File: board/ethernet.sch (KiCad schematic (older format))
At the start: 61 parts, among them IC5 KSZ8081RNx, IC6 MAX5969x, IC7 MAX17503, J1 RJHSE-538B, T1 749010012A, Y2 25MHz

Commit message: Made capacitors more consistent in vals+fps
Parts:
- C23, C25: footprint agg:1206 -> agg:0603; Farnell (none) -> 2494232
- C29, C30, C31, C32: Farnell (none) -> 1828955
- C35: value C -> 10u
- C38: Farnell (none) -> 2579024
- C40: Farnell (none) -> 2496941
- C41: value 2u -> 2u2; footprint agg:1206 -> agg:0603; Farnell (none) -> 1735526
- C43: Farnell (none) -> 1735526
- R24: value 3M3 -> 2M; Farnell (none) -> 2502428
- R27: Farnell 2059687 -> 2502428
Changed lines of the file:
@@
 F 2 "agg:0805" H 2788 2850 50  0001 C CNN
 F 3 "" H 2750 3000 50  0000 C CNN
+F 4 "1828955" H 2750 3000 60  0001 C CNN "Farnell"
 	1    2750 3000
 	1    0    0    -1
@@
 F 0 "C25" H 6565 1596 50  0000 L CNN
 F 1 "22u" H 6565 1505 50  0000 L CNN
-F 2 "agg:1206" H 6488 1400 50  0001 C CNN
+F 2 "agg:0603" H 6488 1400 50  0001 C CNN
 F 3 "" H 6450 1550 50  0000 C CNN
+F 4 "2494232" H 6450 1550 60  0001 C CNN "Farnell"
 	1    6450 1550
 	1    0    0    -1
@@
 P 10200 3200
 F 0 "C35" H 10315 3246 50  0000 L CNN
-F 1 "C" H 10315 3155 50  0000 L CNN
+F 1 "10u" H 10315 3155 50  0000 L CNN
 F 2 "agg:0603" H 10238 3050 50  0001 C CNN
 F 3 "" H 10200 3200 50  0000 C CNN
@@
 F 2 "agg:0805" H 3188 2850 50  0001 C CNN
 F 3 "" H 3150 3000 50  0000 C CNN
+F 4 "1828955" H 3150 3000 60  0001 C CNN "Farnell"
 	1    3150 3000
 	1    0    0    -1
@@
 F 2 "agg:0805" H 3588 2850 50  0001 C CNN
 F 3 "" H 3550 3000 50  0000 C CNN
+F 4 "1828955" H 3550 3000 60  0001 C CNN "Farnell"
 	1    3550 3000
 	1    0    0    -1
@@
 F 2 "agg:0805" H 3988 2850 50  0001 C CNN
 F 3 "" H 3950 3000 50  0000 C CNN
+F 4 "1828955" H 3950 3000 60  0001 C CNN "Farnell"
 	1    3950 3000
 	1    0    0    -1
@@
 F 0 "C23" H 6565 1046 50  0000 L CNN
 F 1 "22u" H 6565 955 50  0000 L CNN
-F 2 "agg:1206" H 6488 850 50  0001 C CNN
+F 2 "agg:0603" H 6488 850 50  0001 C CNN
 F 3 "" H 6450 1000 50  0000 C CNN
+F 4 "2494232" H 6450 1000 60  0001 C CNN "Farnell"
 	1    6450 1000
 	1    0    0    -1
@@
 F 1 "2u2 60V" H 6450 4350 50  0000 L CNN
 F 2 "agg:1210" H 6438 4300 50  0001 C CNN
-F 3 "" H 6400 4450 50  0000 C CNN
+F 3 "http://www.farnell.com/datasheets/2205011.pdf" H 6400 4450 50  0001 C CNN
+F 4 "2579024" H 6400 4450 60  0001 C CNN "Farnell"
 	1    6400 4450
 	-1   0    0    1
@@
 P 5900 4750
 F 0 "R24" H 5959 4796 50  0000 L CNN
-F 1 "3M3" H 5959 4705 50  0000 L CNN
+F 1 "2M" H 5959 4705 50  0000 L CNN
 F 2 "agg:0603" H 5900 4750 50  0001 C CNN
-F 3 "" H 5900 4750 50  0000 C CNN
+F 3 "http://www.farnell.com/datasheets/1960319.pdf" H 5900 4750 50  0001 C CNN
+F 4 "2502428" H 5900 4750 60  0001 C CNN "Farnell"
 	1    5900 4750
 	1    0    0    -1
@@
 F 1 "2u2" H 8365 5905 50  0000 L CNN
 F 2 "agg:0603" H 8288 5800 50  0001 C CNN
-F 3 "" H 8250 5950 50  0000 C CNN
+F 3 "http://www.farnell.com/datasheets/2048825.pdf" H 8250 5950 50  0001 C CNN
+F 4 "1735526" H 8250 5950 60  0001 C CNN "Farnell"
 	1    8250 5950
 	1    0    0    -1
@@
 P 8900 5200
 F 0 "C41" H 9015 5246 50  0000 L CNN
-F 1 "2u" H 9015 5155 50  0000 L CNN
-F 2 "agg:1206" H 8938 5050 50  0001 C CNN
-F 3 "" H 8900 5200 50  0000 C CNN
+F 1 "2u2" H 9015 5155 50  0000 L CNN
+F 2 "agg:0603" H 8938 5050 50  0001 C CNN
+F 3 "http://www.farnell.com/datasheets/2048825.pdf" H 8900 5200 50  0001 C CNN
+F 4 "1735526" H 8900 5200 60  0001 C CNN "Farnell"
 	1    8900 5200
 	1    0    0    -1
@@
 F 1 "2M" H 9420 5305 50  0000 L CNN
 F 2 "agg:0603" V 9280 5350 50  0001 C CNN
-F 3 "" H 9350 5350 50  0000 C CNN
-F 4 "2059687" H 9350 5350 60  0001 C CNN "Farnell"
+F 3 "http://www.farnell.com/datasheets/1960319.pdf" H 9350 5350 50  0001 C CNN
+F 4 "2502428" H 9350 5350 60  0001 C CNN "Farnell"
 	1    9350 5350
 	1    0    0    -1
@@
 F 1 "100n 60V" H 2865 5055 50  0000 L CNN
 F 2 "agg:0805" H 2788 4950 50  0001 C CNN
-F 3 "" H 2750 5100 50  0000 C CNN
+F 3 "http://www.farnell.com/datasheets/1958513.pdf" H 2750 5100 50  0001 C CNN
+F 4 "2496941" H 2750 5100 60  0001 C CNN "Farnell"
 	1    2750 5100
 	1    0    0    -1

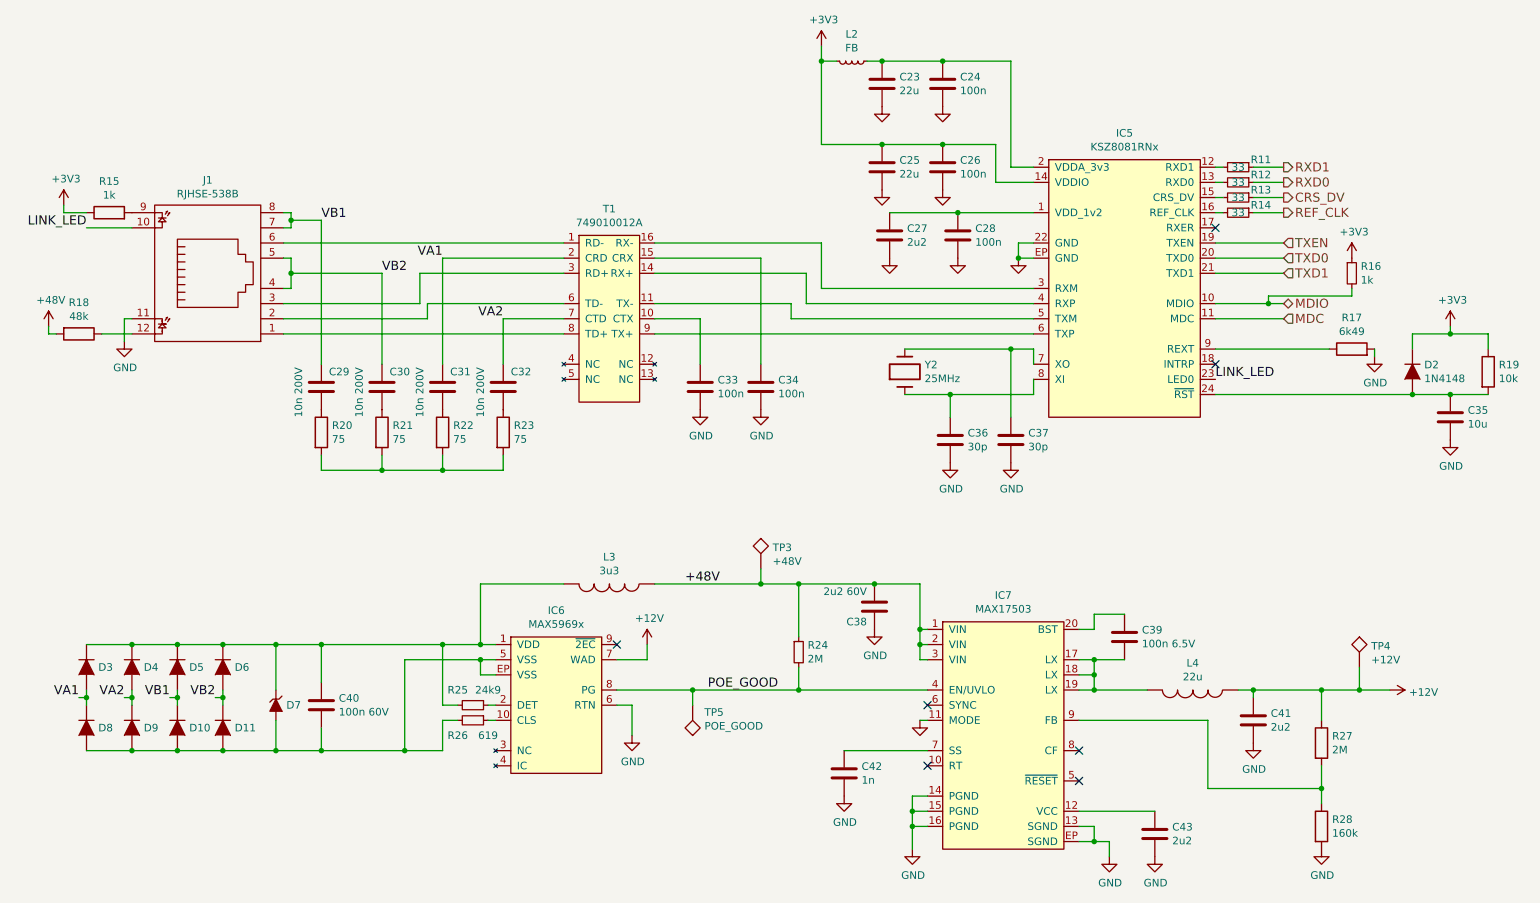
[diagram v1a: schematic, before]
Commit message: Fixed ERC with liberal application of pwr_flag
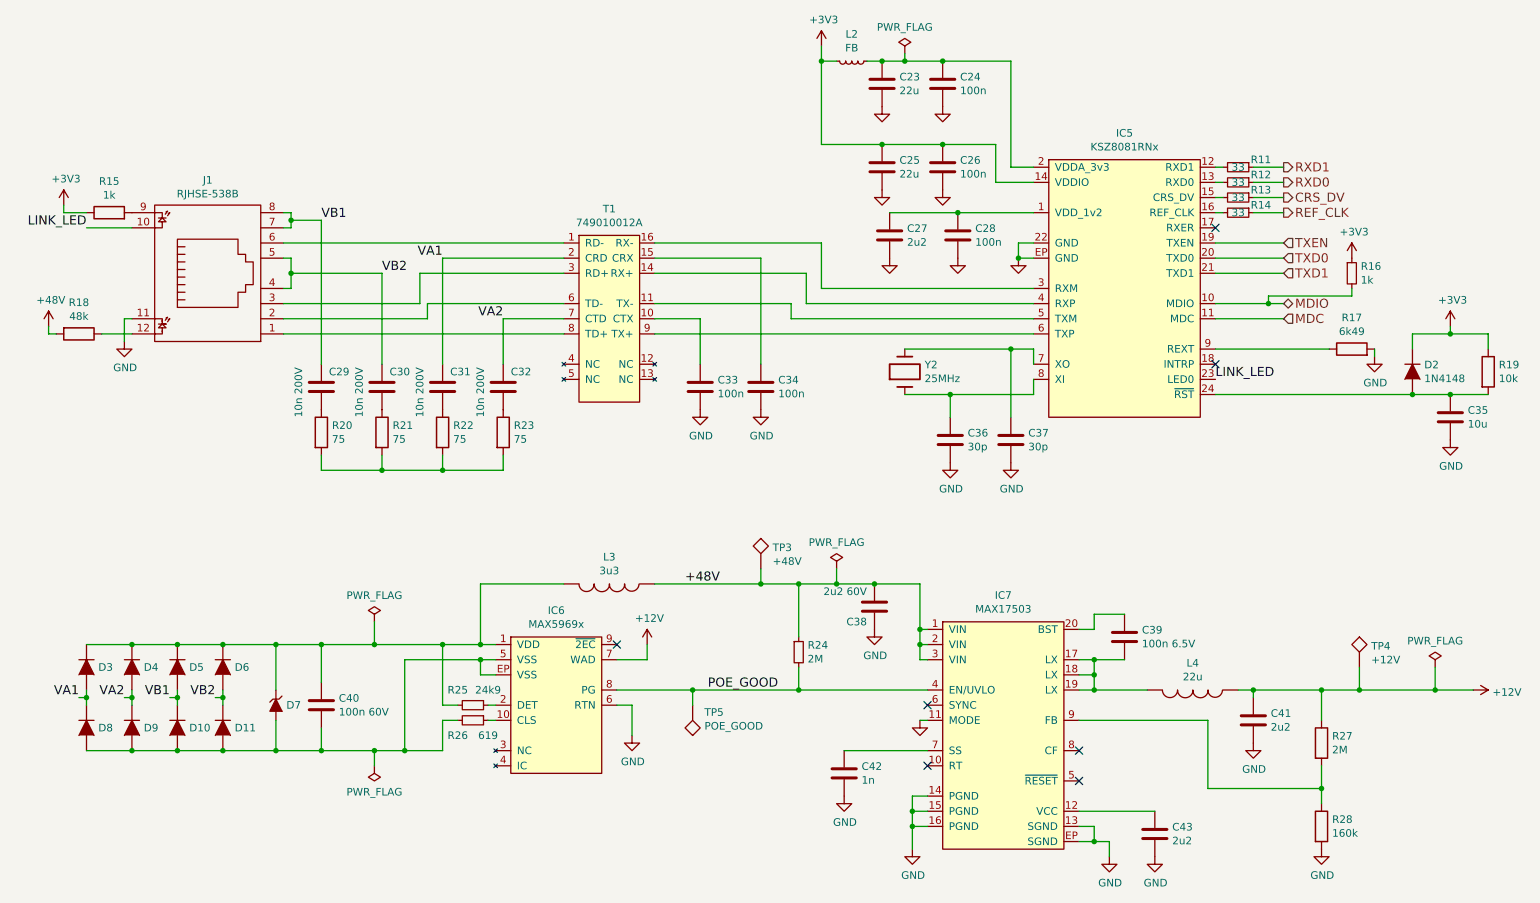
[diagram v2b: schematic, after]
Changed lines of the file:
@@
 LINK_LED
 $Comp
-L +3V3 #PWR041
+L +3V3 #PWR042
 U 1 1 58B9F35C
 P 1050 1800
-F 0 "#PWR041" H 1050 1650 50  0001 C CNN
+F 0 "#PWR042" H 1050 1650 50  0001 C CNN
 F 1 "+3V3" H 1065 1973 50  0000 C CNN
 F 2 "" H 1050 1800 50  0000 C CNN
@@
 $EndComp
 $Comp
-L GND #PWR042
+L GND #PWR043
 U 1 1 58BA0647
 P 5250 3150
-F 0 "#PWR042" H 5250 2900 50  0001 C CNN
+F 0 "#PWR043" H 5250 2900 50  0001 C CNN
 F 1 "GND" H 5255 2977 50  0000 C CNN
 F 2 "" H 5250 3150 50  0000 C CNN
@@
 $EndComp
 $Comp
-L GND #PWR043
+L GND #PWR044
 U 1 1 58BA068E
 P 5650 3150
-F 0 "#PWR043" H 5650 2900 50  0001 C CNN
+F 0 "#PWR044" H 5650 2900 50  0001 C CNN
 F 1 "GND" H 5655 2977 50  0000 C CNN
 F 2 "" H 5650 3150 50  0000 C CNN
@@
 $EndComp
 $Comp
-L GND #PWR044
+L GND #PWR045
 U 1 1 58BA115A
 P 7350 2150
-F 0 "#PWR044" H 7350 1900 50  0001 C CNN
+F 0 "#PWR045" H 7350 1900 50  0001 C CNN
 F 1 "GND" H 7355 1977 50  0001 C CNN
 F 2 "" H 7350 2150 50  0000 C CNN
@@
 $EndComp
 $Comp
-L GND #PWR045
+L GND #PWR046
 U 1 1 58BA1640
 P 6900 3500
-F 0 "#PWR045" H 6900 3250 50  0001 C CNN
+F 0 "#PWR046" H 6900 3250 50  0001 C CNN
 F 1 "GND" H 6905 3327 50  0000 C CNN
 F 2 "" H 6900 3500 50  0000 C CNN
@@
 $EndComp
 $Comp
-L GND #PWR046
+L GND #PWR047
 U 1 1 58BA1690
 P 7300 3500
-F 0 "#PWR046" H 7300 3250 50  0001 C CNN
+F 0 "#PWR047" H 7300 3250 50  0001 C CNN
 F 1 "GND" H 7305 3327 50  0000 C CNN
 F 2 "" H 7300 3500 50  0000 C CNN
@@
 $EndComp
 $Comp
-L GND #PWR047
+L GND #PWR048
 U 1 1 58BA1A5E
 P 6500 2150
-F 0 "#PWR047" H 6500 1900 50  0001 C CNN
+F 0 "#PWR048" H 6500 1900 50  0001 C CNN
 F 1 "GND" H 6505 1977 50  0001 C CNN
 F 2 "" H 6500 2150 50  0000 C CNN
@@
 $EndComp
 $Comp
-L GND #PWR048
+L GND #PWR049
 U 1 1 58BA1AB4
 P 6950 2150
-F 0 "#PWR048" H 6950 1900 50  0001 C CNN
+F 0 "#PWR049" H 6950 1900 50  0001 C CNN
 F 1 "GND" H 6955 1977 50  0001 C CNN
 F 2 "" H 6950 2150 50  0000 C CNN
@@
 $EndComp
 $Comp
-L +3V3 #PWR049
+L +3V3 #PWR050
 U 1 1 58BA1E02
 P 6050 750
-F 0 "#PWR049" H 6050 600 50  0001 C CNN
+F 0 "#PWR050" H 6050 600 50  0001 C CNN
 F 1 "+3V3" H 6065 923 50  0000 C CNN
 F 2 "" H 6050 750 50  0000 C CNN
@@
 $EndComp
 $Comp
-L GND #PWR050
+L GND #PWR051
 U 1 1 58BA48D5
 P 6450 1150
-F 0 "#PWR050" H 6450 900 50  0001 C CNN
+F 0 "#PWR051" H 6450 900 50  0001 C CNN
 F 1 "GND" H 6455 977 50  0001 C CNN
 F 2 "" H 6450 1150 50  0000 C CNN
@@
 $EndComp
 $Comp
-L GND #PWR051
+L GND #PWR052
 U 1 1 58BA492B
 P 6850 1150
-F 0 "#PWR051" H 6850 900 50  0001 C CNN
+F 0 "#PWR052" H 6850 900 50  0001 C CNN
 F 1 "GND" H 6855 977 50  0001 C CNN
 F 2 "" H 6850 1150 50  0000 C CNN
@@
 $EndComp
 $Comp
-L GND #PWR052
+L GND #PWR053
 U 1 1 58BA4B25
 P 6450 1700
-F 0 "#PWR052" H 6450 1450 50  0001 C CNN
+F 0 "#PWR053" H 6450 1450 50  0001 C CNN
 F 1 "GND" H 6455 1527 50  0001 C CNN
 F 2 "" H 6450 1700 50  0000 C CNN
@@
 $EndComp
 $Comp
-L GND #PWR053
+L GND #PWR054
 U 1 1 58BA4BE5
 P 6850 1700
-F 0 "#PWR053" H 6850 1450 50  0001 C CNN
+F 0 "#PWR054" H 6850 1450 50  0001 C CNN
 F 1 "GND" H 6855 1527 50  0001 C CNN
 F 2 "" H 6850 1700 50  0000 C CNN
@@
 $EndComp
 $Comp
-L +3V3 #PWR054
+L +3V3 #PWR055
 U 1 1 58BA8C0B
 P 9550 2150
-F 0 "#PWR054" H 9550 2000 50  0001 C CNN
+F 0 "#PWR055" H 9550 2000 50  0001 C CNN
 F 1 "+3V3" H 9565 2323 50  0000 C CNN
 F 2 "" H 9550 2150 50  0000 C CNN
@@
 $EndComp
 $Comp
-L GND #PWR055
+L GND #PWR056
 U 1 1 58BABD3E
 P 9700 2800
-F 0 "#PWR055" H 9700 2550 50  0001 C CNN
+F 0 "#PWR056" H 9700 2550 50  0001 C CNN
 F 1 "GND" H 9705 2627 50  0000 C CNN
 F 2 "" H 9700 2800 50  0000 C CNN
@@
 $EndComp
 $Comp
-L +3V3 #PWR056
+L +3V3 #PWR057
 U 1 1 58BAD620
 P 10200 2600
-F 0 "#PWR056" H 10200 2450 50  0001 C CNN
+F 0 "#PWR057" H 10200 2450 50  0001 C CNN
 F 1 "+3V3" H 10215 2773 50  0000 C CNN
 F 2 "" H 10200 2600 50  0000 C CNN
@@
 $EndComp
 $Comp
-L GND #PWR057
+L GND #PWR058
 U 1 1 58BAD7C0
 P 10200 3350
-F 0 "#PWR057" H 10200 3100 50  0001 C CNN
+F 0 "#PWR058" H 10200 3100 50  0001 C CNN
 F 1 "GND" H 10205 3177 50  0000 C CNN
 F 2 "" H 10200 3350 50  0000 C CNN
@@
 NoConn ~ 4700 4700
 $Comp
-L GND #PWR058
+L GND #PWR059
 U 1 1 58BC4A36
 P 4800 5300
-F 0 "#PWR058" H 4800 5050 50  0001 C CNN
+F 0 "#PWR059" H 4800 5050 50  0001 C CNN
 F 1 "GND" H 4805 5127 50  0000 C CNN
 F 2 "" H 4800 5300 50  0000 C CNN
@@
 $EndComp
 $Comp
-L GND #PWR059
+L GND #PWR060
 U 1 1 58BC73C0
 P 6400 4600
-F 0 "#PWR059" H 6400 4350 50  0001 C CNN
+F 0 "#PWR060" H 6400 4350 50  0001 C CNN
 F 1 "GND" H 6405 4427 50  0000 C CNN
 F 2 "" H 6400 4600 50  0000 C CNN
@@
 NoConn ~ 6750 5100
 $Comp
-L GND #PWR060
+L GND #PWR061
 U 1 1 58BC9E72
 P 6700 5200
-F 0 "#PWR060" H 6700 4950 50  0001 C CNN
+F 0 "#PWR061" H 6700 4950 50  0001 C CNN
 F 1 "GND" H 6705 5027 50  0001 C CNN
 F 2 "" H 6700 5200 50  0000 C CNN
@@
 $EndComp
 $Comp
-L GND #PWR061
+L GND #PWR062
 U 1 1 58BCA458
 P 6200 5700
-F 0 "#PWR061" H 6200 5450 50  0001 C CNN
+F 0 "#PWR062" H 6200 5450 50  0001 C CNN
 F 1 "GND" H 6205 5527 50  0000 C CNN
 F 2 "" H 6200 5700 50  0000 C CNN
@@
 NoConn ~ 6750 5500
 $Comp
-L GND #PWR062
+L GND #PWR063
 U 1 1 58BCAA6F
 P 6650 6050
-F 0 "#PWR062" H 6650 5800 50  0001 C CNN
+F 0 "#PWR063" H 6650 5800 50  0001 C CNN
 F 1 "GND" H 6655 5877 50  0000 C CNN
 F 2 "" H 6650 6050 50  0000 C CNN
@@
 NoConn ~ 7750 5600
 $Comp
-L GND #PWR063
+L GND #PWR064
 U 1 1 58BCCF2C
 P 7950 6100
-F 0 "#PWR063" H 7950 5850 50  0001 C CNN
+F 0 "#PWR064" H 7950 5850 50  0001 C CNN
 F 1 "GND" H 7955 5927 50  0000 C CNN
 F 2 "" H 7950 6100 50  0000 C CNN
@@
 $EndComp
 $Comp
-L GND #PWR064
+L GND #PWR065
 U 1 1 58BCD1A4
 P 8250 6100
-F 0 "#PWR064" H 8250 5850 50  0001 C CNN
+F 0 "#PWR065" H 8250 5850 50  0001 C CNN
 F 1 "GND" H 8255 5927 50  0000 C CNN
 F 2 "" H 8250 6100 50  0000 C CNN
@@
 $EndComp
 $Comp
-L GND #PWR065
+L GND #PWR066
 U 1 1 58BCDD4D
 P 8900 5350
-F 0 "#PWR065" H 8900 5100 50  0001 C CNN
+F 0 "#PWR066" H 8900 5100 50  0001 C CNN
 F 1 "GND" H 8905 5177 50  0000 C CNN
 F 2 "" H 8900 5350 50  0000 C CNN
@@
 $EndComp
 $Comp
-L GND #PWR066
+L GND #PWR067
 U 1 1 58BCE5C3
 P 9350 6050
-F 0 "#PWR066" H 9350 5800 50  0001 C CNN
+F 0 "#PWR067" H 9350 5800 50  0001 C CNN
 F 1 "GND" H 9355 5877 50  0000 C CNN
 F 2 "" H 9350 6050 50  0000 C CNN
@@
 $EndComp
 $Comp
-L +12V #PWR067
+L +12V #PWR068
 U 1 1 58BCF882
-P 9800 5000
-F 0 "#PWR067" H 9800 4850 50  0001 C CNN
-F 1 "+12V" V 9815 5128 50  0000 L CNN
-F 2 "" H 9800 5000 50  0000 C CNN
-F 3 "" H 9800 5000 50  0000 C CNN
-	1    9800 5000
+P 10350 5000
+F 0 "#PWR068" H 10350 4850 50  0001 C CNN
+F 1 "+12V" V 10365 5128 50  0000 L CNN
+F 2 "" H 10350 5000 50  0000 C CNN
+F 3 "" H 10350 5000 50  0000 C CNN
+	1    10350 5000
 	0    1    1    0
 $EndComp
@@
 Connection ~ 5900 5000
 Wire Wire Line
-	8800 5000 9800 5000
+	8800 5000 10350 5000
 Wire Wire Line
 	9350 5650 8600 5650
 $Comp
-L +12V #PWR068
+L +12V #PWR069
 U 1 1 58BC71BD
 P 4900 4700
-F 0 "#PWR068" H 4900 4550 50  0001 C CNN
+F 0 "#PWR069" H 4900 4550 50  0001 C CNN
 F 1 "+12V" H 4915 4873 50  0000 C CNN
 F 2 "" H 4900 4700 50  0000 C CNN
@@
 Connection ~ 5200 5000
 $Comp
-L +48V #PWR069
+L +48V #PWR070
 U 1 1 58DB5468
 P 950 2600
-F 0 "#PWR069" H 950 2450 50  0001 C CNN
+F 0 "#PWR070" H 950 2450 50  0001 C CNN
 F 1 "+48V" H 965 2773 50  0000 C CNN
 F 2 "" H 950 2600 50  0001 C CNN
@@
 $EndComp
 $Comp
-L GND #PWR070
+L GND #PWR071
 U 1 1 58DB5B5A
 P 1450 2700
-F 0 "#PWR070" H 1450 2450 50  0001 C CNN
+F 0 "#PWR071" H 1450 2450 50  0001 C CNN
 F 1 "GND" H 1455 2527 50  0000 C CNN
 F 2 "" H 1450 2700 50  0001 C CNN
@@
 Wire Wire Line
 	1050 1850 1200 1850
+$Comp
+L PWR_FLAG #FLG072
+U 0 1 58E0F72D
+P 10100 4850
+F 0 "#FLG072" H 10100 4925 50  0001 C CNN
+F 1 "PWR_FLAG" H 10100 5024 50  0000 C CNN
+F 2 "" H 10100 4850 50  0001 C CNN
+F 3 "" H 10100 4850 50  0001 C CNN
+	0    10100 4850
+	1    0    0    -1
+$EndComp
+Wire Wire Line
+	10100 4850 10100 5000
+Connection ~ 10100 5000
+$Comp
+L PWR_FLAG #FLG073
+U 0 1 58E11EB9
+P 3100 4550
+F 0 "#FLG073" H 3100 4625 50  0001 C CNN
+F 1 "PWR_FLAG" H 3100 4724 50  0000 C CNN
+F 2 "" H 3100 4550 50  0001 C CNN
+F 3 "" H 3100 4550 50  0001 C CNN
+	0    3100 4550
+	1    0    0    -1
+$EndComp
+Wire Wire Line
+	3100 4550 3100 4700
+Connection ~ 3100 4700
+$Comp
+L PWR_FLAG #FLG074
+U 0 1 58E13788
+P 3100 5500
+F 0 "#FLG074" H 3100 5575 50  0001 C CNN
+F 1 "PWR_FLAG" H 3100 5673 50  0000 C CNN
+F 2 "" H 3100 5500 50  0001 C CNN
+F 3 "" H 3100 5500 50  0001 C CNN
+	0    3100 5500
+	-1   0    0    1
+$EndComp
+Wire Wire Line
+	3100 5500 3100 5400
+Connection ~ 3100 5400
+$Comp
+L PWR_FLAG #FLG075
+U 0 1 58E16BA0
+P 6150 4200
+F 0 "#FLG075" H 6150 4275 50  0001 C CNN
+F 1 "PWR_FLAG" H 6150 4374 50  0000 C CNN
+F 2 "" H 6150 4200 50  0001 C CNN
+F 3 "" H 6150 4200 50  0001 C CNN
+	0    6150 4200
+	1    0    0    -1
+$EndComp
+Wire Wire Line
+	6150 4200 6150 4300
+Connection ~ 6150 4300
+$Comp
+L PWR_FLAG #FLG076
+U 0 1 58E174E3
+P 6600 800
+F 0 "#FLG076" H 6600 875 50  0001 C CNN
+F 1 "PWR_FLAG" H 6600 974 50  0000 C CNN
+F 2 "" H 6600 800 50  0001 C CNN
+F 3 "" H 6600 800 50  0001 C CNN
+	0    6600 800
+	1    0    0    -1
+$EndComp
+Wire Wire Line
+	6600 800  6600 850
+Connection ~ 6600 850
 $EndSCHEMATC

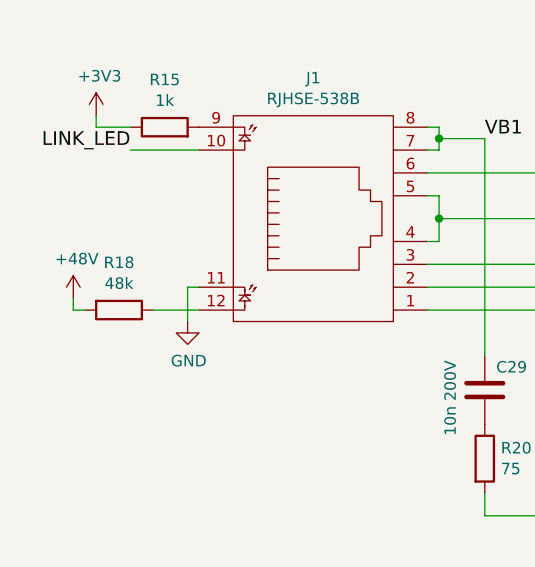
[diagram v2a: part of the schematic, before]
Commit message: Tidied top half of board
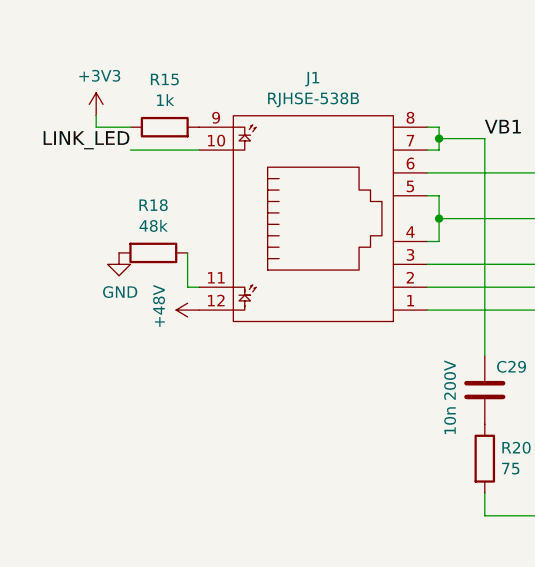
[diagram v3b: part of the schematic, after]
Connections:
- net +48V: now also J1.12; no longer R18.2
- net GND: now also R18.2; no longer J1.11
- net at R18.1: now also J1.11; no longer J1.12
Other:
- moved on the sheet: R18
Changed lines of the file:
@@
 L +48V #PWR070
 U 1 1 58DB5468
-P 950 2600
-F 0 "#PWR070" H 950 2450 50  0001 C CNN
-F 1 "+48V" H 965 2773 50  0000 C CNN
-F 2 "" H 950 2600 50  0001 C CNN
-F 3 "" H 950 2600 50  0001 C CNN
-	1    950  2600
-	1    0    0    -1
+P 1500 2650
+F 0 "#PWR070" H 1500 2500 50  0001 C CNN
+F 1 "+48V" H 1515 2823 50  0000 C CNN
+F 2 "" H 1500 2650 50  0001 C CNN
+F 3 "" H 1500 2650 50  0001 C CNN
+	1    1500 2650
+	0    -1   -1   0
 $EndComp
 $Comp
 L R R18
 U 1 1 58DB5701
-P 1150 2650
-F 0 "R18" V 943 2650 50  0000 C CNN
-F 1 "48k" V 1034 2650 50  0000 C CNN
-F 2 "agg:0603" V 1080 2650 50  0001 C CNN
-F 3 "" H 1150 2650 50  0001 C CNN
-	1    1150 2650
+P 1300 2400
+F 0 "R18" V 1093 2400 50  0000 C CNN
+F 1 "48k" V 1184 2400 50  0000 C CNN
+F 2 "agg:0603" V 1230 2400 50  0001 C CNN
+F 3 "" H 1300 2400 50  0001 C CNN
+	1    1300 2400
 	0    1    1    0
 $EndComp
@@
 L GND #PWR071
 U 1 1 58DB5B5A
-P 1450 2700
-F 0 "#PWR071" H 1450 2450 50  0001 C CNN
-F 1 "GND" H 1455 2527 50  0000 C CNN
-F 2 "" H 1450 2700 50  0001 C CNN
-F 3 "" H 1450 2700 50  0001 C CNN
-	1    1450 2700
+P 1150 2400
+F 0 "#PWR071" H 1150 2150 50  0001 C CNN
+F 1 "GND" H 1155 2227 50  0000 C CNN
+F 2 "" H 1150 2400 50  0001 C CNN
+F 3 "" H 1150 2400 50  0001 C CNN
+	1    1150 2400
 	1    0    0    -1
 $EndComp
-Wire Wire Line
-	950  2600 950  2650
-Wire Wire Line
-	950  2650 1000 2650
-Wire Wire Line
-	1300 2650 1500 2650
-Wire Wire Line
-	1500 2550 1450 2550
-Wire Wire Line
-	1450 2550 1450 2700
 Wire Wire Line
 	1050 1800 1050 1850
@@
 	6600 800  6600 850
 Connection ~ 6600 850
+Wire Wire Line
+	1500 2550 1450 2550
+Wire Wire Line
+	1450 2550 1450 2400
 $EndSCHEMATC
